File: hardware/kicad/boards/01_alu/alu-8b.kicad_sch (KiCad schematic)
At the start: 97 parts, among them J1 Conn_01x35, J2 Conn_01x24, U17 74HC540, U18 74HC540, U19 74HC182, U20 74HC182, U21 74HC182, U22 74HC157, U23 74HC157, U24 74HC244, U25 74HC4078, U26 74AHC1G86, U27 74HC244, U28 74HC244, U29 74HC244, U30 74HC244

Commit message: feat: designed alu0-control unit and wired on top level of 32b alu
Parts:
- removed C17, C18, C19, C20, C21, C22, C23, C26, C27, C28, C29, C30, C31, C32: 100nF, Capacitor_SMD:C_0603_1608Metric, symbol Device:C
- removed C24, C25: C, Capacitor_SMD:C_0603_1608Metric, symbol Device:C
- removed D1, D10, D11, D12, D13, D14, D15, D16, D17, D18, D19, D2, D20, D21, D22, D3, D4, D5, D6, D7, D8, D9: LED, LED_SMD:LED_0805_2012Metric, symbol Device:LED
- removed J1: Conn_01x35, Connector_PinHeader_2.54mm:PinHeader_1x35_P2.54mm_Vertical, symbol Connector_Generic:Conn_01x35
- removed J2: Conn_01x24, Connector_PinHeader_2.54mm:PinHeader_1x24_P2.54mm_Vertical, symbol Connector_Generic:Conn_01x24
- removed R1, R2, R3, R4: 1000, Resistor_SMD:R_0603_1608Metric, symbol Device:R
- removed R10, R11, R12, R13, R14, R15, R16, R17, R18, R19, R20, R21, R22, R23, R24, R25, R26, R5, R6, R7, R8, R9: 2200, Resistor_SMD:R_0805_2012Metric, symbol Device:R
- removed TP1, TP10, TP11, TP12, TP13, TP14, TP15, TP16, TP17, TP2, TP3, TP4, TP5, TP6, TP7, TP8, TP9: TestPoint, TestPoint:TestPoint_Pad_1.0x1.0mm, symbol Connector:TestPoint
- removed U17, U18: 74HC540, Package_SO:SOIC-20W_7.5x12.8mm_P1.27mm, symbol 74xx:74LS540
- removed U19, U20, U21: 74HC182, Package_SO:SOIC-16_3.9x9.9mm_P1.27mm, symbol 74xx:74LS182
- removed U22, U23: 74HC157, Package_SO:SOIC-16_3.9x9.9mm_P1.27mm, symbol 74xx:74LS157
- removed U24, U27, U28, U29, U30: 74HC244, Package_SO:SOIC-20W_7.5x12.8mm_P1.27mm, symbol 74xx:74LS244
- removed U25: 74HC4078, Package_SO:SOIC-14_3.9x8.7mm_P1.27mm, symbol 4xxx_IEEE:4078
- removed U26: 74AHC1G86, Package_TO_SOT_SMD:SOT-23-5, symbol 74xGxx:74AHC1G86
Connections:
- no-connect marks 3 -> 0
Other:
- removed sheet 1b_alu_slice_1
- removed sheet 1b_alu_slice_2
- removed sheet 1b_alu_slice_3
- removed sheet 1b_alu_slice_4
- removed sheet 1b_alu_slice_5
- removed sheet 1b_alu_slice_6
- removed sheet 1b_alu_slice_7
- removed sheet 1b_alu_slice_8
- removed sheet alu-1b1
- removed sheet alu-1b2
- removed sheet alu-1b3
- removed sheet alu-1b4
- removed sheet alu-1b5
- removed sheet alu-1b6
- removed sheet alu-1b7
- removed sheet alu-1b8
- added sheet alu-1b-0 (alu-1b.kicad_sch)
- added sheet alu-1b-1 (alu-1b.kicad_sch)
- added sheet alu-1b-2 (alu-1b.kicad_sch)
- added sheet alu-1b-3 (alu-1b.kicad_sch)
- added sheet alu-1b-4 (alu-1b.kicad_sch)
- added sheet alu-1b-5 (alu-1b.kicad_sch)
- added sheet alu-1b-6 (alu-1b.kicad_sch)
- added sheet alu-1b-7 (alu-1b.kicad_sch)

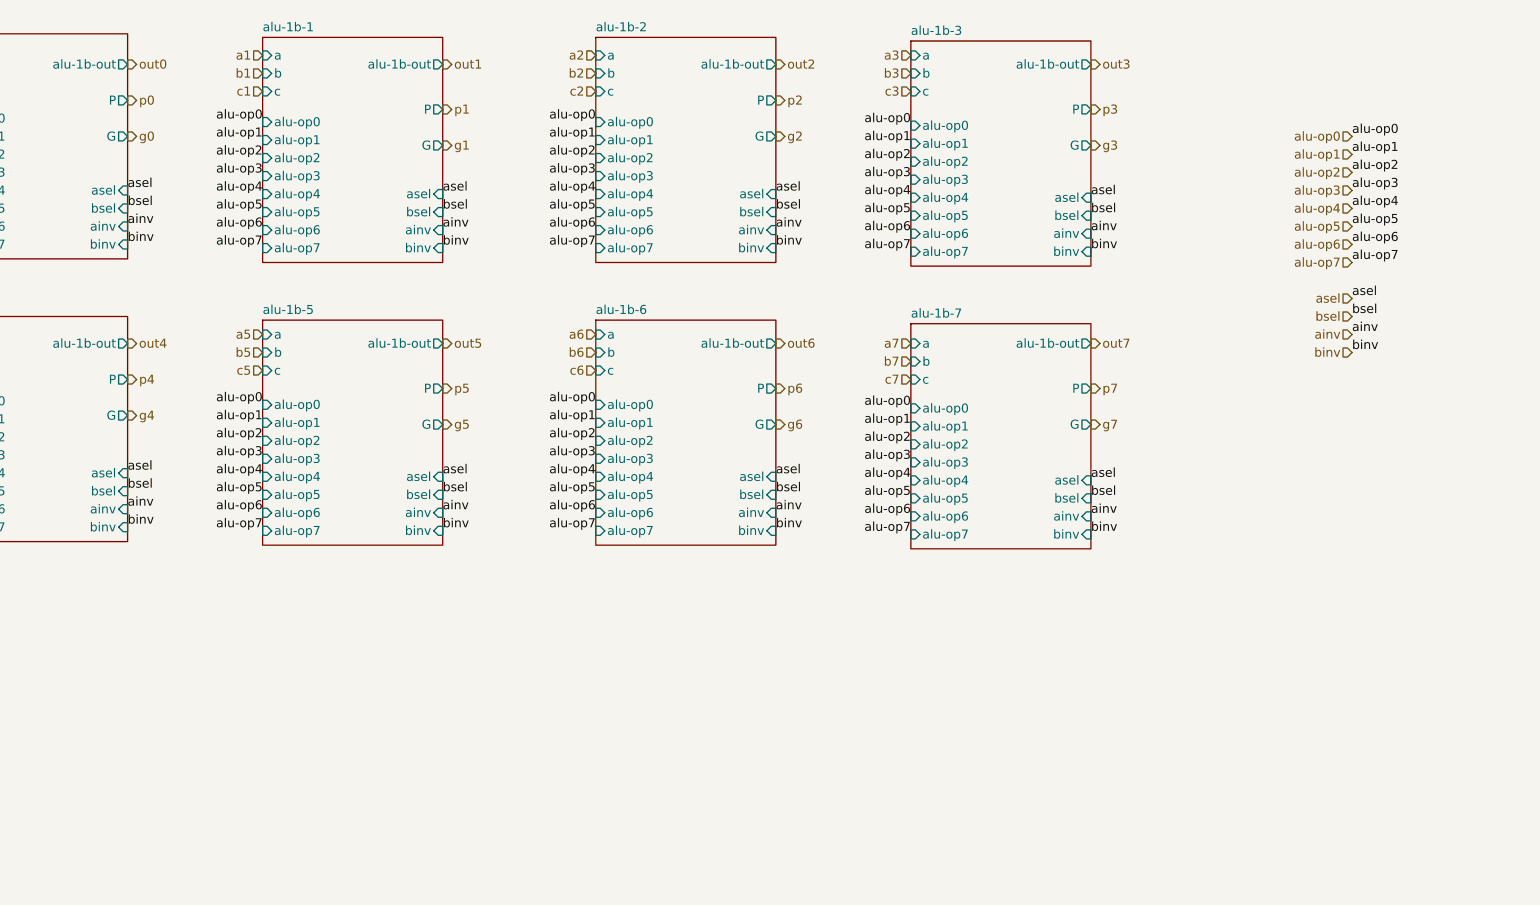
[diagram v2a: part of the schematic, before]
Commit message: kicad: checkpoint; designed the alu display logic; clock circuit
Added registers for each display to ensure robustness and less worry about debugging screen, keeping focus on the alu board and other components
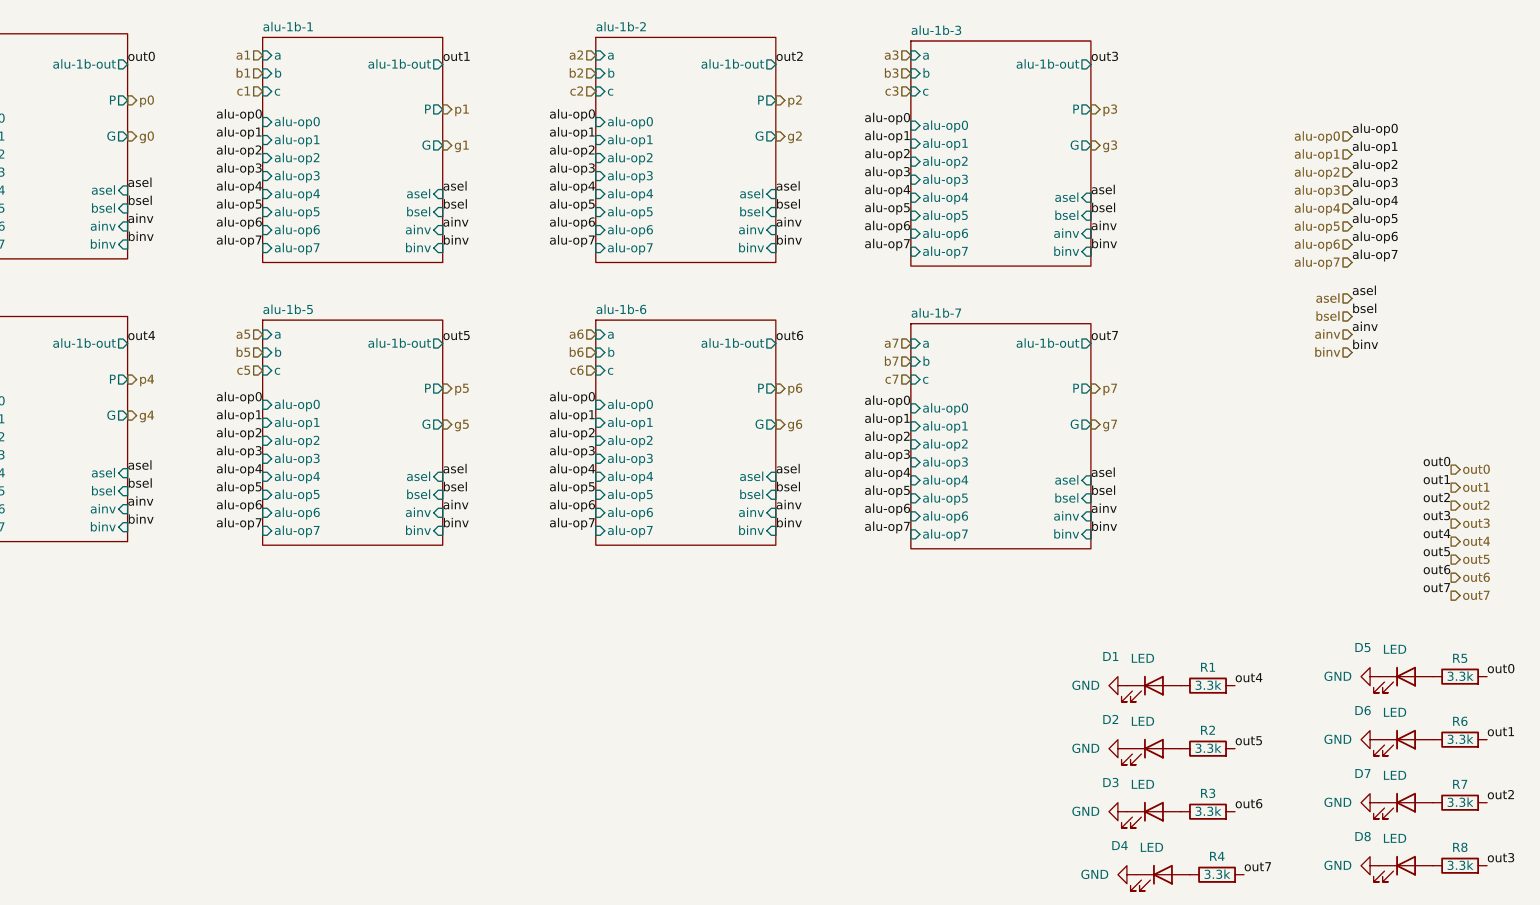
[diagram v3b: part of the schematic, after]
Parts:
- added D1, D2, D3, D4, D5, D6, D7, D8: LED, LED_THT:LED_D5.0mm, symbol Device:LED
- added R1, R2, R3, R4, R5, R6, R7, R8: 3.3k, Resistor_SMD:R_0805_2012Metric, symbol Device:R
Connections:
- net out0: now also R5.2
- net out1: now also R6.2
- net out2: now also R7.2
- net out3: now also R8.2
- net out4: now also R1.2
- net out5: now also R2.2
- net out6: now also R3.2
- net out7: now also R4.2
- new net: D6.2 (A), R6.1
- new net: D7.2 (A), R7.1
- new net: D8.2 (A), R8.1
- new net: D1.2 (A), R1.1
- new net: D5.2 (A), R5.1
- new net: D3.2 (A), R3.1
- new net: D2.2 (A), R2.1
- new net: D4.2 (A), R4.1
- new net GND: D1.1 (K), D2.1 (K), D3.1 (K), D4.1 (K), D5.1 (K), D6.1 (K), D7.1 (K), D8.1 (K)

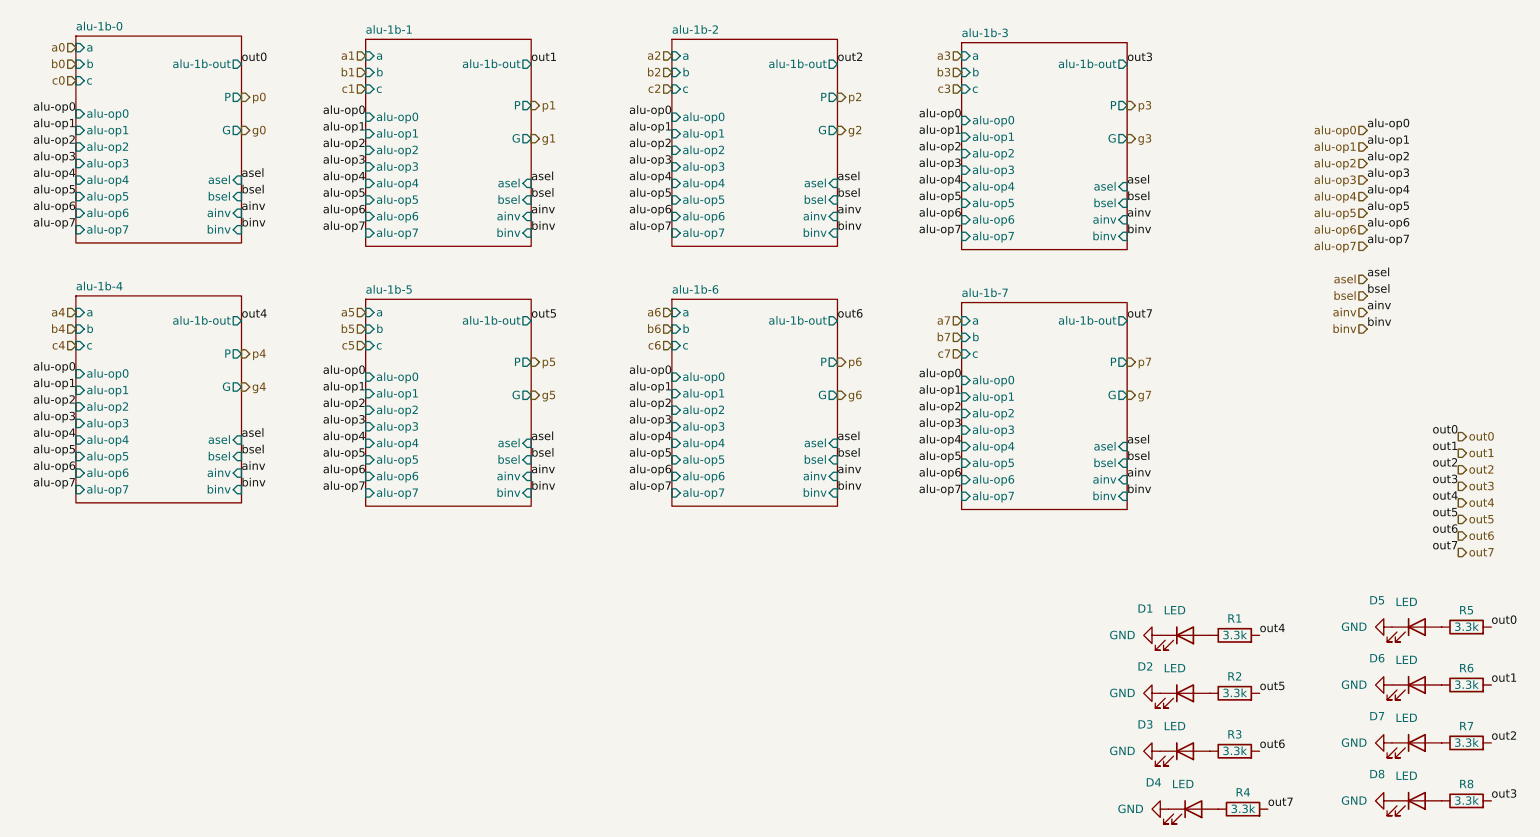
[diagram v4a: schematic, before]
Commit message: refactor: changed hpins to global for asel, ainv, precondition, alu-opcode
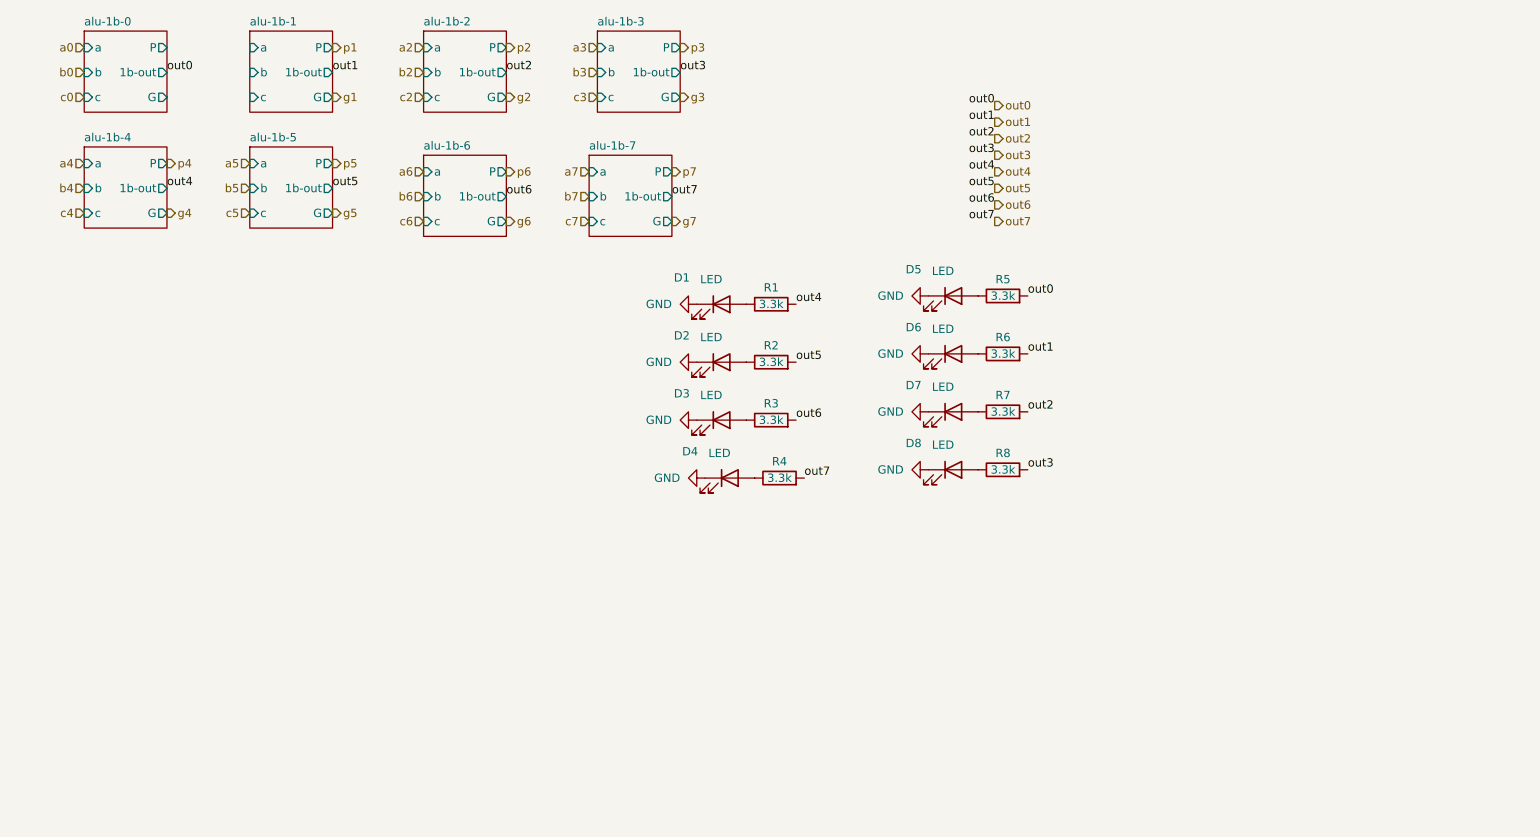
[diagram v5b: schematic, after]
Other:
- sheet alu-1b-0 ports: added 1b-out; removed ainv, alu-1b-out, alu-op0, alu-op1, alu-op2, alu-op3, alu-op4, alu-op5, alu-op6, alu-op7, asel, binv, bsel
- sheet alu-1b-1 ports: added 1b-out; removed ainv, alu-1b-out, alu-op0, alu-op1, alu-op2, alu-op3, alu-op4, alu-op5, alu-op6, alu-op7, asel, binv, bsel
- sheet alu-1b-2 ports: added 1b-out; removed ainv, alu-1b-out, alu-op0, alu-op1, alu-op2, alu-op3, alu-op4, alu-op5, alu-op6, alu-op7, asel, binv, bsel
- sheet alu-1b-3 ports: added 1b-out; removed ainv, alu-1b-out, alu-op0, alu-op1, alu-op2, alu-op3, alu-op4, alu-op5, alu-op6, alu-op7, asel, binv, bsel
- sheet alu-1b-4 ports: added 1b-out; removed ainv, alu-1b-out, alu-op0, alu-op1, alu-op2, alu-op3, alu-op4, alu-op5, alu-op6, alu-op7, asel, binv, bsel
- sheet alu-1b-5 ports: added 1b-out; removed ainv, alu-1b-out, alu-op0, alu-op1, alu-op2, alu-op3, alu-op4, alu-op5, alu-op6, alu-op7, asel, binv, bsel
- sheet alu-1b-6 ports: added 1b-out; removed ainv, alu-1b-out, alu-op0, alu-op1, alu-op2, alu-op3, alu-op4, alu-op5, alu-op6, alu-op7, asel, binv, bsel
- sheet alu-1b-7 ports: added 1b-out; removed ainv, alu-1b-out, alu-op0, alu-op1, alu-op2, alu-op3, alu-op4, alu-op5, alu-op6, alu-op7, asel, binv, bsel
- moved on the sheet: D1, D2, D3, D4, D5, D6, D7, D8, R1, R2, R3, R4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

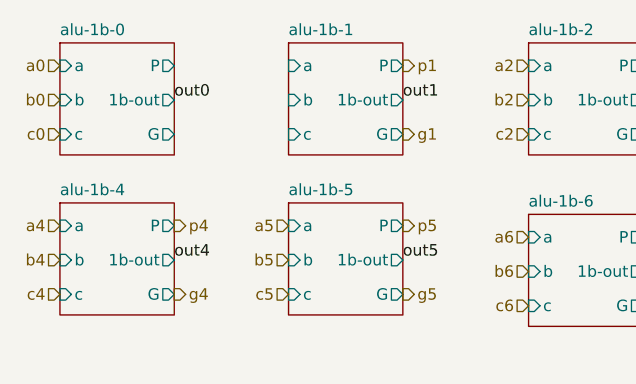
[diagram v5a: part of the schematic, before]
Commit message: refactor: improved global labeling and reduced ERC from 300+ to 6 power flags and minor connector in errors
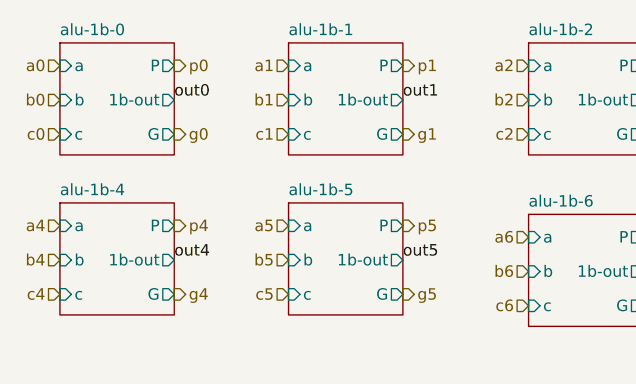
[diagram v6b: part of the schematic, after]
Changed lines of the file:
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@@
+		)
+	)
+	(hierarchical_label "c1"
+		(shape input)
+		(at 67.31 40.64 180)
+		(effects
+			(font
+				(size 1.27 1.27)
+			)
+			(justify right)
 		)
 	)
@@
 		)
 	)
+	(hierarchical_label "b1"
+		(shape input)
+		(at 67.31 36.83 180)
+		(effects
+			(font
+				(size 1.27 1.27)
+			)
+			(justify right)
+		)
+	)
 	(hierarchical_label "p4"
 		(shape output)
@@
 		)
 	)
+	(hierarchical_label "g0"
+		(shape output)
+		(at 54.61 40.64 0)
+		(effects
+			(font
+				(size 1.27 1.27)
+			)
+			(justify left)
+		)
+	)
 	(hierarchical_label "g2"
 		(shape output)
@@
 		)
 	)
+	(hierarchical_label "a1"
+		(shape input)
+		(at 67.31 33.02 180)
+		(effects
+			(font
+				(size 1.27 1.27)
+			)
+			(justify right)
+		)
+	)
 	(hierarchical_label "b6"
 		(shape input)
@@
 		(effects
 			(font
+				(size 1.27 1.27)
+			)
+			(justify left)
+		)
+	)
+	(hierarchical_label "p0"
+		(shape output)
+		(at 54.61 33.02 0)
+		(effects
+			(font
